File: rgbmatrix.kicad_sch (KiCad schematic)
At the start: 132 parts

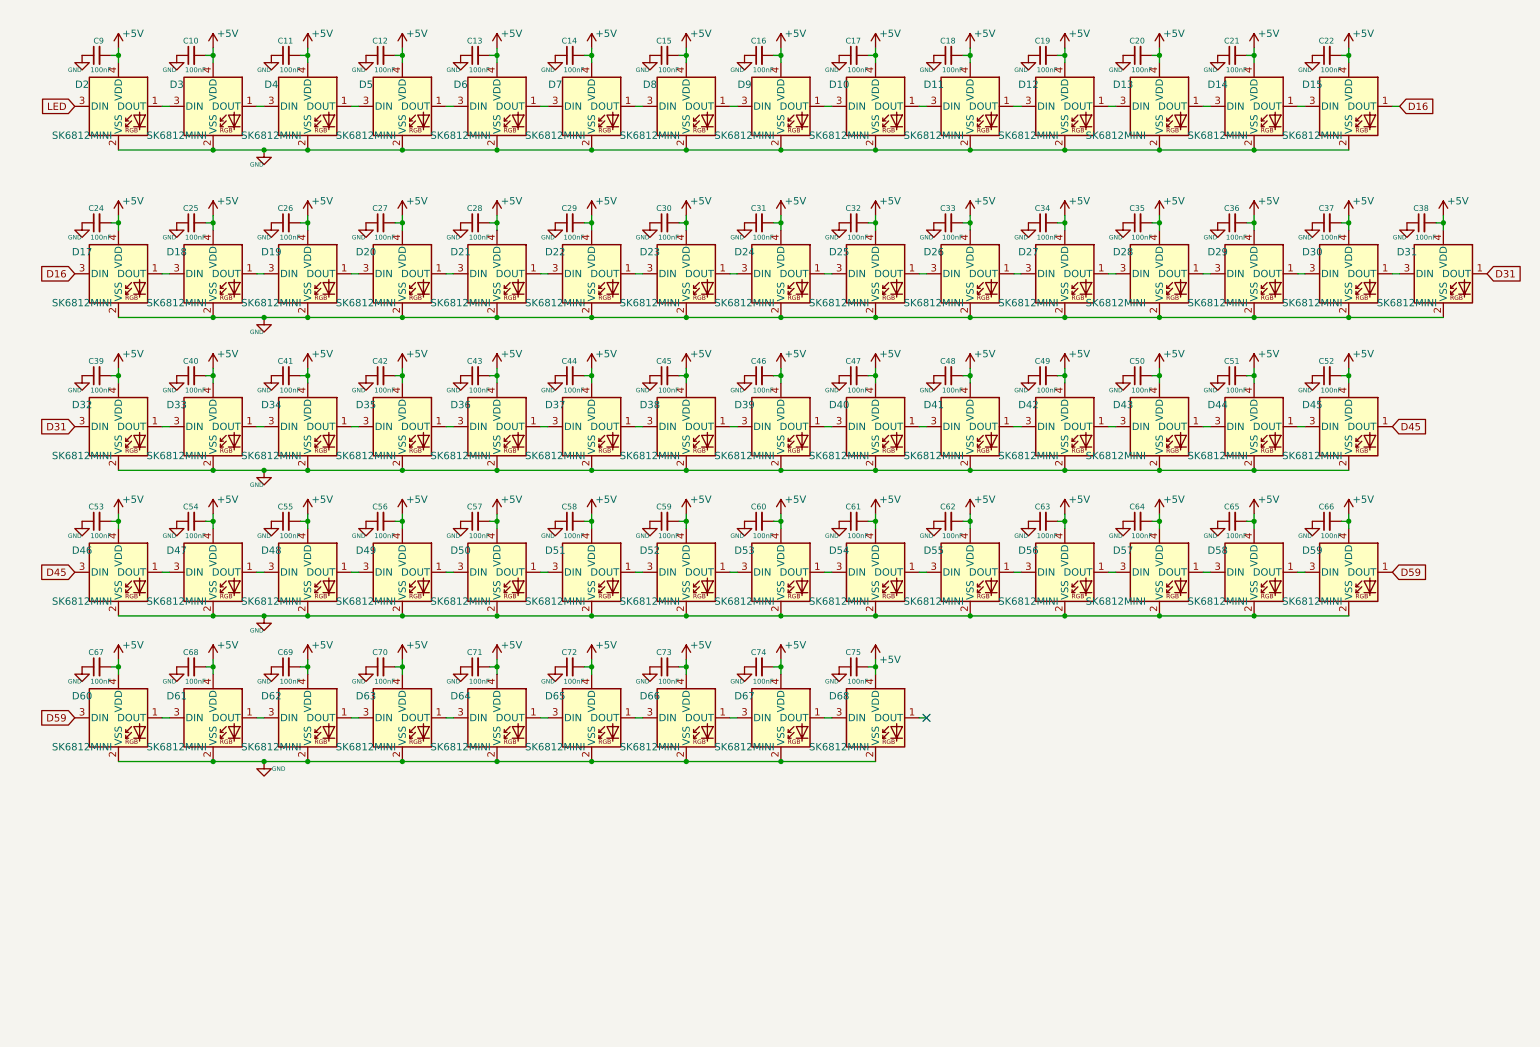
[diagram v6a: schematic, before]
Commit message: changed LEDs fr, added deb to switch
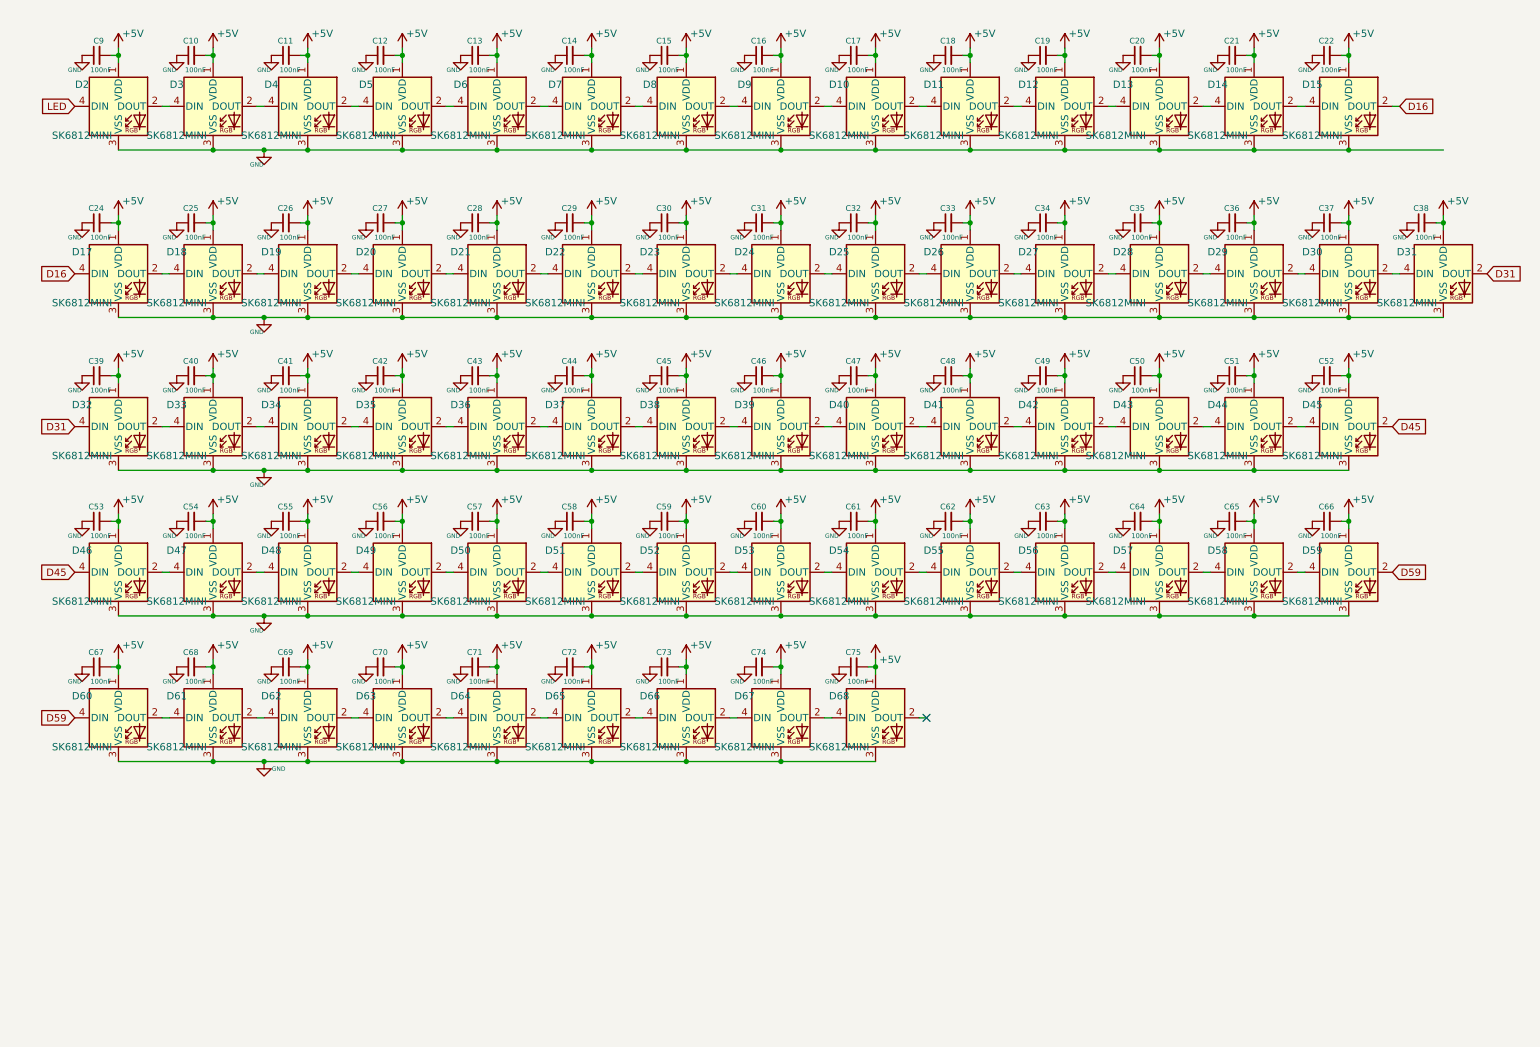
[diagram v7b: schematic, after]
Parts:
- D10, D11, D12, D13, D14, D15, D17, D18, D19, D2, D20, D21, D22, D23, D24, D25, D26, D27, D28, D29, D3, D30, D31, D32, D33, D34, D35, D36, D37, D38, D39, D4, D40, D41, D42, D43, D44, D45, D46, D47, D48, D49, D5, D50, D51, D52, D53, D54, D55, D56, D57, D58, D59, D6, D60, D61, D62, D63, D64, D65, D66, D67, D68, D7, D8, D9: footprint reverse:MX_SK6812MINI-E_REV -> personalLibrary:MX_SK6812MINI-E_REV; symbol LED:SK6812MINI -> reverseneocringething:SK6812_REVERSE
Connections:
- net +5V: now also D10.1 (VDD), D11.1 (VDD), D12.1 (VDD), D13.1 (VDD), D14.1 (VDD), D15.1 (VDD), D17.1 (VDD), D18.1 (VDD), D19.1 (VDD), D2.1 (VDD), D20.1 (VDD), D21.1 (VDD), D22.1 (VDD), D23.1 (VDD), D24.1 (VDD), D25.1 (VDD), D26.1 (VDD), D27.1 (VDD), D28.1 (VDD), D29.1 (VDD), D3.1 (VDD), D30.1 (VDD), D31.1 (VDD), D32.1 (VDD), D33.1 (VDD), D34.1 (VDD), D35.1 (VDD), D36.1 (VDD), D37.1 (VDD), D38.1 (VDD), D39.1 (VDD), D4.1 (VDD), D40.1 (VDD), D41.1 (VDD), D42.1 (VDD), D43.1 (VDD), D44.1 (VDD), D45.1 (VDD), D46.1 (VDD), D47.1 (VDD), D48.1 (VDD), D49.1 (VDD), D5.1 (VDD), D50.1 (VDD), D51.1 (VDD), D52.1 (VDD), D53.1 (VDD), D54.1 (VDD), D55.1 (VDD), D56.1 (VDD), D57.1 (VDD), D58.1 (VDD), D59.1 (VDD), D6.1 (VDD), D60.1 (VDD), D61.1 (VDD), D62.1 (VDD), D63.1 (VDD), D64.1 (VDD), D65.1 (VDD), D66.1 (VDD), D67.1 (VDD), D68.1 (VDD), D7.1 (VDD), D8.1 (VDD), D9.1 (VDD); no longer D10.4 (VDD), D11.4 (VDD), D12.4 (VDD), D13.4 (VDD), D14.4 (VDD), D15.4 (VDD), D17.4 (VDD), D18.4 (VDD), D19.4 (VDD), D2.4 (VDD), D20.4 (VDD), D21.4 (VDD), D22.4 (VDD), D23.4 (VDD), D24.4 (VDD), D25.4 (VDD), D26.4 (VDD), D27.4 (VDD), D28.4 (VDD), D29.4 (VDD), D3.4 (VDD), D30.4 (VDD), D31.4 (VDD), D32.4 (VDD), D33.4 (VDD), D34.4 (VDD), D35.4 (VDD), D36.4 (VDD), D37.4 (VDD), D38.4 (VDD), D39.4 (VDD), D4.4 (VDD), D40.4 (VDD), D41.4 (VDD), D42.4 (VDD), D43.4 (VDD), D44.4 (VDD), D45.4 (VDD), D46.4 (VDD), D47.4 (VDD), D48.4 (VDD), D49.4 (VDD), D5.4 (VDD), D50.4 (VDD), D51.4 (VDD), D52.4 (VDD), D53.4 (VDD), D54.4 (VDD), D55.4 (VDD), D56.4 (VDD), D57.4 (VDD), D58.4 (VDD), D59.4 (VDD), D6.4 (VDD), D60.4 (VDD), D61.4 (VDD), D62.4 (VDD), D63.4 (VDD), D64.4 (VDD), D65.4 (VDD), D66.4 (VDD), D67.4 (VDD), D68.4 (VDD), D7.4 (VDD), D8.4 (VDD), D9.4 (VDD)
- net D16: now also D15.2 (DOUT), D17.4 (DIN); no longer D15.1 (DOUT), D17.3 (DIN)
- net D31: now also D31.2 (DOUT), D32.4 (DIN); no longer D31.1 (DOUT), D32.3 (DIN)
- net D45: now also D45.2 (DOUT), D46.4 (DIN); no longer D45.1 (DOUT), D46.3 (DIN)
- net D59: now also D59.2 (DOUT), D60.4 (DIN); no longer D59.1 (DOUT), D60.3 (DIN)
- net GND: now also D10.3 (VSS), D11.3 (VSS), D12.3 (VSS), D13.3 (VSS), D14.3 (VSS), D15.3 (VSS), D17.3 (VSS), D18.3 (VSS), D19.3 (VSS), D2.3 (VSS), D20.3 (VSS), D21.3 (VSS), D22.3 (VSS), D23.3 (VSS), D24.3 (VSS), D25.3 (VSS), D26.3 (VSS), D27.3 (VSS), D28.3 (VSS), D29.3 (VSS), D3.3 (VSS), D30.3 (VSS), D31.3 (VSS), D32.3 (VSS), D33.3 (VSS), D34.3 (VSS), D35.3 (VSS), D36.3 (VSS), D37.3 (VSS), D38.3 (VSS), D39.3 (VSS), D4.3 (VSS), D40.3 (VSS), D41.3 (VSS), D42.3 (VSS), D43.3 (VSS), D44.3 (VSS), D45.3 (VSS), D46.3 (VSS), D47.3 (VSS), D48.3 (VSS), D49.3 (VSS), D5.3 (VSS), D50.3 (VSS), D51.3 (VSS), D52.3 (VSS), D53.3 (VSS), D54.3 (VSS), D55.3 (VSS), D56.3 (VSS), D57.3 (VSS), D58.3 (VSS), D59.3 (VSS), D6.3 (VSS), D60.3 (VSS), D61.3 (VSS), D62.3 (VSS), D63.3 (VSS), D64.3 (VSS), D65.3 (VSS), D66.3 (VSS), D67.3 (VSS), D68.3 (VSS), D7.3 (VSS), D8.3 (VSS), D9.3 (VSS); no longer D10.2 (VSS), D11.2 (VSS), D12.2 (VSS), D13.2 (VSS), D14.2 (VSS), D15.2 (VSS), D17.2 (VSS), D18.2 (VSS), D19.2 (VSS), D2.2 (VSS), D20.2 (VSS), D21.2 (VSS), D22.2 (VSS), D23.2 (VSS), D24.2 (VSS), D25.2 (VSS), D26.2 (VSS), D27.2 (VSS), D28.2 (VSS), D29.2 (VSS), D3.2 (VSS), D30.2 (VSS), D31.2 (VSS), D32.2 (VSS), D33.2 (VSS), D34.2 (VSS), D35.2 (VSS), D36.2 (VSS), D37.2 (VSS), D38.2 (VSS), D39.2 (VSS), D4.2 (VSS), D40.2 (VSS), D41.2 (VSS), D42.2 (VSS), D43.2 (VSS), D44.2 (VSS), D45.2 (VSS), D46.2 (VSS), D47.2 (VSS), D48.2 (VSS), D49.2 (VSS), D5.2 (VSS), D50.2 (VSS), D51.2 (VSS), D52.2 (VSS), D53.2 (VSS), D54.2 (VSS), D55.2 (VSS), D56.2 (VSS), D57.2 (VSS), D58.2 (VSS), D59.2 (VSS), D6.2 (VSS), D60.2 (VSS), D61.2 (VSS), D62.2 (VSS), D63.2 (VSS), D64.2 (VSS), D65.2 (VSS), D66.2 (VSS), D67.2 (VSS), D68.2 (VSS), D7.2 (VSS), D8.2 (VSS), D9.2 (VSS)
- net LED: now also D2.4 (DIN); no longer D2.3 (DIN)
- new net: D23.2 (DOUT), D24.4 (DIN)
- new net: D22.2 (DOUT), D23.4 (DIN)
- new net: D42.2 (DOUT), D43.4 (DIN)
- new net: D41.2 (DOUT), D42.4 (DIN)
- new net: D21.2 (DOUT), D22.4 (DIN)
- new net: D14.2 (DOUT), D15.4 (DIN)
- new net: D13.2 (DOUT), D14.4 (DIN)
- new net: D10.2 (DOUT), D11.4 (DIN)
- new net: D10.4 (DIN), D9.2 (DOUT)
- new net: D55.2 (DOUT), D56.4 (DIN)
- new net: D54.2 (DOUT), D55.4 (DIN)
- new net: D33.2 (DOUT), D34.4 (DIN)
- new net: D32.2 (DOUT), D33.4 (DIN)
- new net: D2.2 (DOUT), D3.4 (DIN)
- new net: D48.2 (DOUT), D49.4 (DIN)
- new net: D47.2 (DOUT), D48.4 (DIN)
- new net: D25.2 (DOUT), D26.4 (DIN)
- new net: D24.2 (DOUT), D25.4 (DIN)
- new net: D46.2 (DOUT), D47.4 (DIN)
- new net: D67.2 (DOUT), D68.4 (DIN)
- new net: D56.2 (DOUT), D57.4 (DIN)
- new net: D27.2 (DOUT), D28.4 (DIN)
- new net: D26.2 (DOUT), D27.4 (DIN)
- new net: D40.2 (DOUT), D41.4 (DIN)
- new net: D39.2 (DOUT), D40.4 (DIN)
- new net: D37.2 (DOUT), D38.4 (DIN)
- new net: D36.2 (DOUT), D37.4 (DIN)
- new net: D29.2 (DOUT), D30.4 (DIN)
- new net: D28.2 (DOUT), D29.4 (DIN)
- new net: D57.2 (DOUT), D58.4 (DIN)
- new net: D62.2 (DOUT), D63.4 (DIN)
- new net: D61.2 (DOUT), D62.4 (DIN)
- new net: D35.2 (DOUT), D36.4 (DIN)
- new net: D38.2 (DOUT), D39.4 (DIN)
- new net: D66.2 (DOUT), D67.4 (DIN)
- new net: D34.2 (DOUT), D35.4 (DIN)
- new net: D49.2 (DOUT), D50.4 (DIN)
- new net: D8.2 (DOUT), D9.4 (DIN)
- new net: D53.2 (DOUT), D54.4 (DIN)
- new net: D52.2 (DOUT), D53.4 (DIN)
- new net: D4.2 (DOUT), D5.4 (DIN)
- new net: D3.2 (DOUT), D4.4 (DIN)
- new net: D30.2 (DOUT), D31.4 (DIN)
- new net: D19.2 (DOUT), D20.4 (DIN)
- new net: D18.2 (DOUT), D19.4 (DIN)
- new net: D44.2 (DOUT), D45.4 (DIN)
- new net: D43.2 (DOUT), D44.4 (DIN)
- new net: D64.2 (DOUT), D65.4 (DIN)
- new net: D63.2 (DOUT), D64.4 (DIN)
- new net: D7.2 (DOUT), D8.4 (DIN)
- new net: D6.2 (DOUT), D7.4 (DIN)
- new net: D11.2 (DOUT), D12.4 (DIN)
- new net: D65.2 (DOUT), D66.4 (DIN)
- new net: D58.2 (DOUT), D59.4 (DIN)
- new net: D60.2 (DOUT), D61.4 (DIN)
- new net: D17.2 (DOUT), D18.4 (DIN)
- new net: D51.2 (DOUT), D52.4 (DIN)
- new net: D50.2 (DOUT), D51.4 (DIN)
- new net: D20.2 (DOUT), D21.4 (DIN)
- new net: D12.2 (DOUT), D13.4 (DIN)
- new net: D5.2 (DOUT), D6.4 (DIN)
